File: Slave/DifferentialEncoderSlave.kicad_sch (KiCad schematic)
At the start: 17 parts, among them J1 Conn_01x04, U1 LTC2850xS8, U2 MA730, U3 AZ1117-3.3

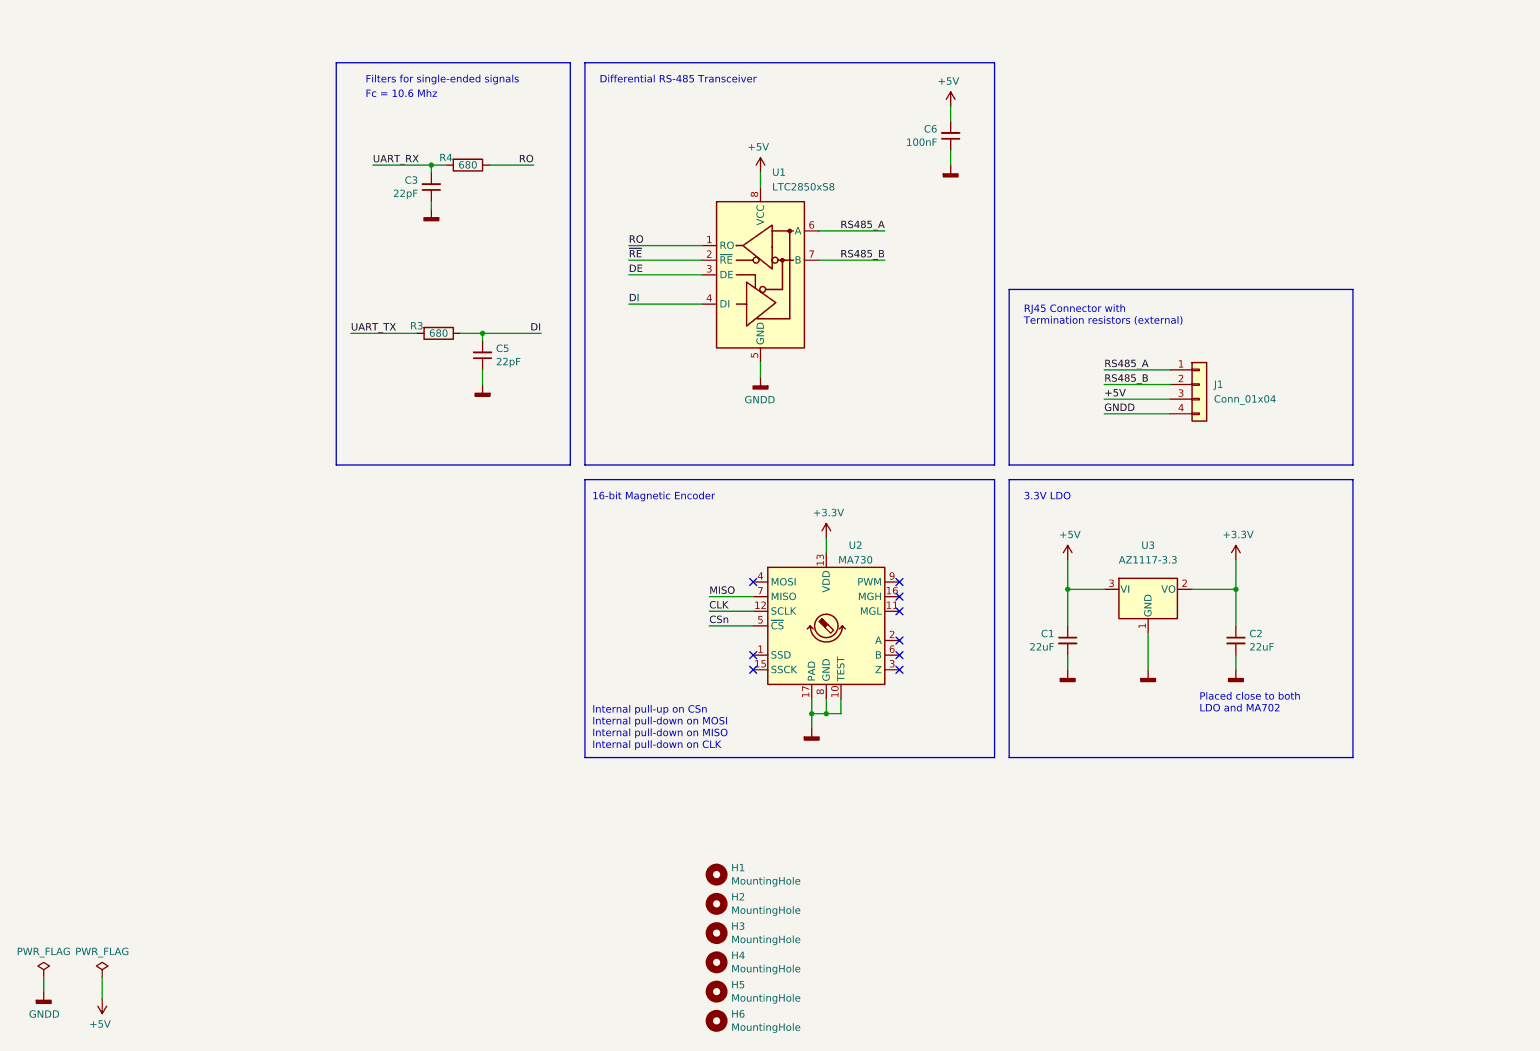
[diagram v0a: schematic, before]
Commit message: Finish laying out encoder board
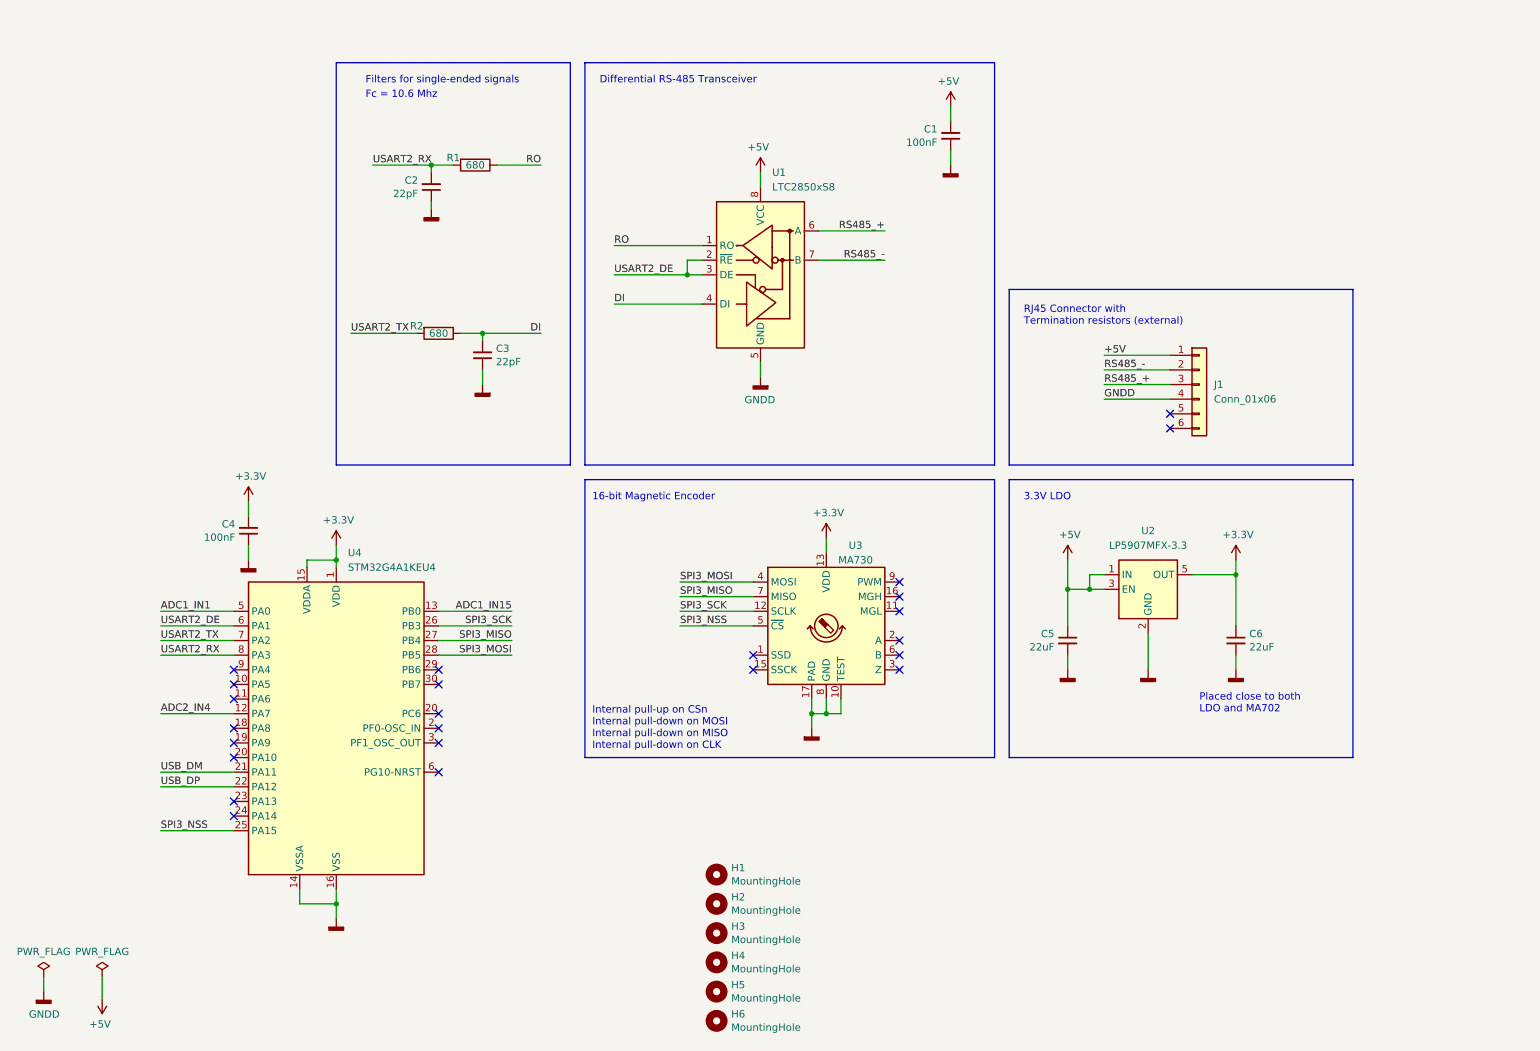
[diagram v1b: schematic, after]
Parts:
- removed J1: Conn_01x04, Connector_JST:JST_PH_S4B-PH-K_1x04_P2.00mm_Horizontal, symbol Connector_Generic:Conn_01x04
- removed U3: AZ1117-3.3, Package_TO_SOT_SMD:SOT-223-3_TabPin2, symbol Regulator_Linear:AZ1117-3.3
- added C4: 100nF, Capacitor_SMD:C_0402_1005Metric, symbol Device:C_Small
- added J1: Conn_01x06, Connector_Molex:Molex_CLIK-Mate_502585-0670_1x06-1MP_P1.50mm_Horizontal, symbol Connector_Generic:Conn_01x06
- added U2: LP5907MFX-3.3, Package_TO_SOT_SMD:SOT-23-5, symbol Regulator_Linear:LP5907MFX-3.3
- added U4: STM32G4A1KEU4, Package_DFN_QFN:UFQFPN-32-1EP_5x5mm_P0.5mm_EP3.5x3.5mm, symbol Wetmelon:STM32G4A1KEU4
- C1: renamed from C6; footprint Capacitor_SMD:C_0603_1608Metric -> Capacitor_SMD:C_0402_1005Metric
- C2: renamed from C3; footprint Capacitor_SMD:C_0603_1608Metric -> Capacitor_SMD:C_0402_1005Metric
- C3: renamed from C5; footprint Capacitor_SMD:C_0603_1608Metric -> Capacitor_SMD:C_0402_1005Metric
- R1: renamed from R4; footprint Resistor_SMD:R_0603_1608Metric -> Resistor_SMD:R_0402_1005Metric
- R2: renamed from R3; footprint Resistor_SMD:R_0603_1608Metric -> Resistor_SMD:R_0402_1005Metric
- renumbered C1 to C5, C2 to C6, U2 to U3
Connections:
- net ~{RE} is gone; now on net USART2_DE: U1.2 (~{RE})
- net +3V3: now also C4.2, U2.5 (OUT), U4.1 (VDD), U4.15 (VDDA), U4.17 (VDD)
- net +5V: now also J1.1 (Pin_1), U2.1 (IN), U2.3 (EN)
- net GNDD: now also C4.1, J1.4 (Pin_4), U2.2 (GND), U4.14 (VSSA), U4.16 (VSS), U4.33 (PAD)
- net SPI3_MOSI: now reaches U3.4 (MOSI)
- net SPI3_MOSI: now also U4.28 (PB5)
- net CLK renamed SPI3_SCK
- net SPI3_SCK: now also U4.26 (PB3)
- net CSn renamed SPI3_NSS
- net SPI3_NSS: now also U4.25 (PA15)
- net DE renamed USART2_DE
- net USART2_DE: now also U4.6 (PG10-NRST)
- net MISO renamed SPI3_MISO
- net SPI3_MISO: now also U4.27 (PB4)
- net RS485_A renamed RS485_+
- net RS485_+: now also J1.3 (Pin_3)
- net RS485_B renamed RS485_-
- net RS485_-: now also J1.2 (Pin_2)
- net UART_RX renamed USART2_RX
- net USART2_RX: now also U4.8 (PA3)
- net UART_TX renamed USART2_TX
- net USART2_TX: now also U4.7 (PA2)
- new net ADC1_IN1: U4.5 (PA0)
- new net ADC1_IN15: U4.13 (PB0)
- new net ADC2_IN4: U4.12 (PA7)
- new net USB_DM: U4.21 (PA11)
- new net USB_DP: U4.22 (PA12)
- no-connect marks 9 -> 24
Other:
- moved on the sheet: R1

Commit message: Change pinout on STM32G4, add thermistor header, add test points
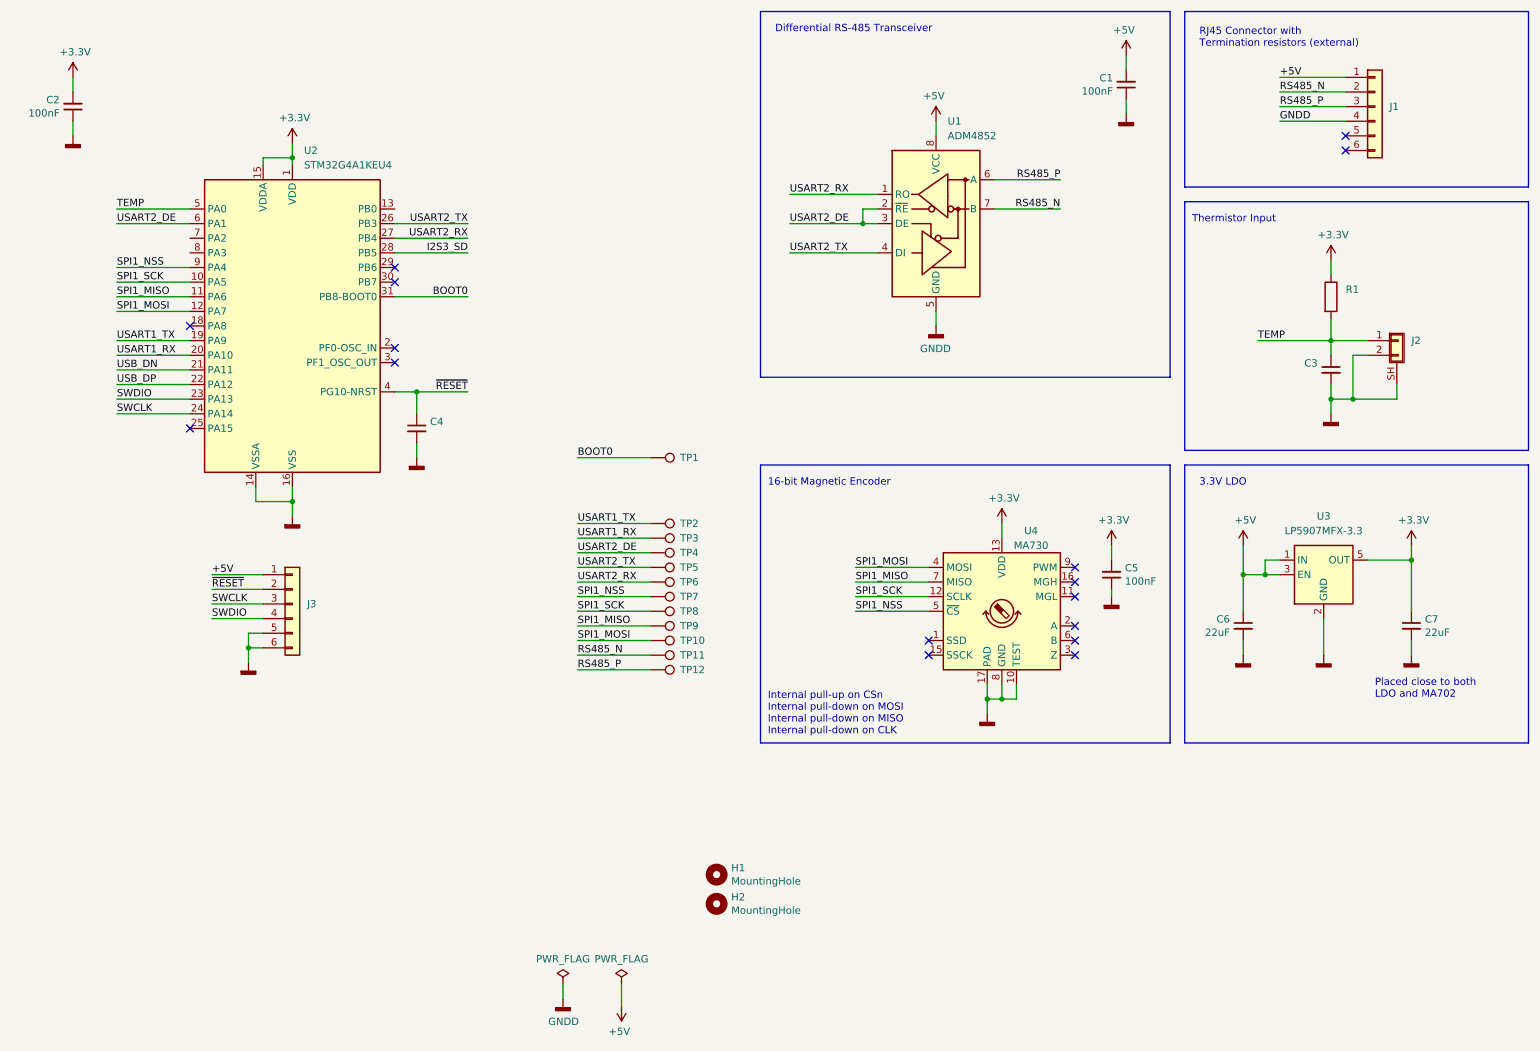
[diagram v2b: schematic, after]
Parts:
- removed C2: 22pF, Capacitor_SMD:C_0402_1005Metric, symbol Device:C_Small
- removed H3, H4: MountingHole, MountingHole:MountingHole_3mm, symbol Mechanical:MountingHole
- removed H5, H6: MountingHole, MountingHole:MountingHole_3.2mm_M3_DIN965, symbol Mechanical:MountingHole
- removed R2: 680, Resistor_SMD:R_0402_1005Metric, symbol Device:R
- added C4: (no value), symbol Device:C_Small
- added C5: 100nF, Capacitor_SMD:C_0402_1005Metric, symbol Device:C_Small
- added J2: (no value), symbol Connector_Generic_Shielded:Conn_01x02_Shielded
- added J3: (no value), symbol Connector_Generic:Conn_01x06
- added TP1, TP10, TP11, TP12, TP2, TP3, TP4, TP5, TP6, TP7, TP8, TP9: TestPoint, symbol Connector:TestPoint
- C3: value 22pF -> (none); footprint Capacitor_SMD:C_0402_1005Metric -> (none)
- J1: value Conn_01x06 -> (none)
- R1: value 680 -> (none); footprint Resistor_SMD:R_0402_1005Metric -> (none)
- U1: value LTC2850xS8 -> ADM4852; footprint Package_SO:SOIC-8_3.9x4.9mm_P1.27mm -> (none)
- renumbered C4 to C2, C5 to C6, C6 to C7, U4 to U2, U2 to U3, U3 to U4
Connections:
- net +3V3: now also R1.1, C5.2
- net +5V: now also J3.1 (Pin_1)
- net GNDD: now also C3.2, U1.PAD, U2.32 (VSS), C4.2, C5.1, J2.2 (Pin_2), J2.SH (Shield), J3.5 (Pin_5), J3.6 (Pin_6); no longer C3.1
- net USART2_DE: now also TP4.1
- net USART2_RX: now also U1.1 (RO), U2.27 (PB4), TP6.1; no longer R1.2, U2.8 (PA3)
- net USART2_TX: now also U1.4 (DI), U2.26 (PB3), TP5.1; no longer U2.7 (PA2)
- net SPI1_SCK: now reaches U2.10 (PA5)
- net SPI1_SCK: now also U4.12 (SCLK), TP8.1
- net SPI1_MISO: now reaches U2.11 (PA6)
- net SPI1_MISO: now also U4.7 (MISO), TP9.1
- net USART1_TX: now reaches U2.19 (PA9)
- net USART1_TX: now also TP2.1
- net USART1_RX: now reaches U2.20 (PA10)
- net USART1_RX: now also TP3.1
- net SWDIO: now reaches U2.23 (PA13)
- net SWDIO: now also J3.4 (Pin_4)
- net SWCLK: now reaches U2.24 (PA14)
- net SWCLK: now also J3.3 (Pin_3)
- net SPI1_NSS: now reaches U2.9 (PA4)
- net SPI1_NSS: now also U4.5 (~{CS}), TP7.1
- net ADC1_IN1 renamed TEMP
- net TEMP: now also C3.1, R1.2, J2.1 (Pin_1)
- net ADC1_IN15: no longer names the net of U2.13 (PB0)
- net ADC2_IN4 renamed SPI1_MOSI
- net SPI1_MOSI: now also U4.4 (MOSI), TP10.1
- removed net DI: C3.2, U1.4 (DI)
- removed net RO: R1.1, U1.1 (RO)
- net RS485_+ renamed RS485_P
- net RS485_P: now also TP12.1
- net RS485_- renamed RS485_N
- net RS485_N: now also TP11.1
- removed net SPI3_MISO: U2.27 (PB4), U4.7 (MISO)
- net SPI3_MOSI renamed I2S3_SD
- net I2S3_SD: no longer U4.4 (MOSI)
- net SPI3_NSS: no longer names the net of U2.25 (PA15)
- net SPI3_NSS: no longer U4.5 (~{CS})
- removed net SPI3_SCK: U2.26 (PB3), U4.12 (SCLK)
- net USB_DM renamed USB_DN
- new net BOOT0: TP1.1, U2.31 (PB8-BOOT0)
- new net ~{RESET}: C4.1, J3.2 (Pin_2), U2.4 (PG10-NRST)
- no-connect marks 24 -> 16
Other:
- note added: "Thermistor Input"
- note removed: "Fc = 10.6 Mhz"
- note removed: "Filters for single-ended signals"
- moved on the sheet: C1, C2, C6, C7, J1, U1, U2, U3, U4
